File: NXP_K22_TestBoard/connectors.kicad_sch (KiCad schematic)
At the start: 22 parts, among them J301 Barrel_Jack, J302 Conn_ARM_JTAG_SWD_10, J303 PortA, J304 PortB, J305 PortC, J306 PortD, J307 Analog, J308 OLED, J309 UART, J310 Power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

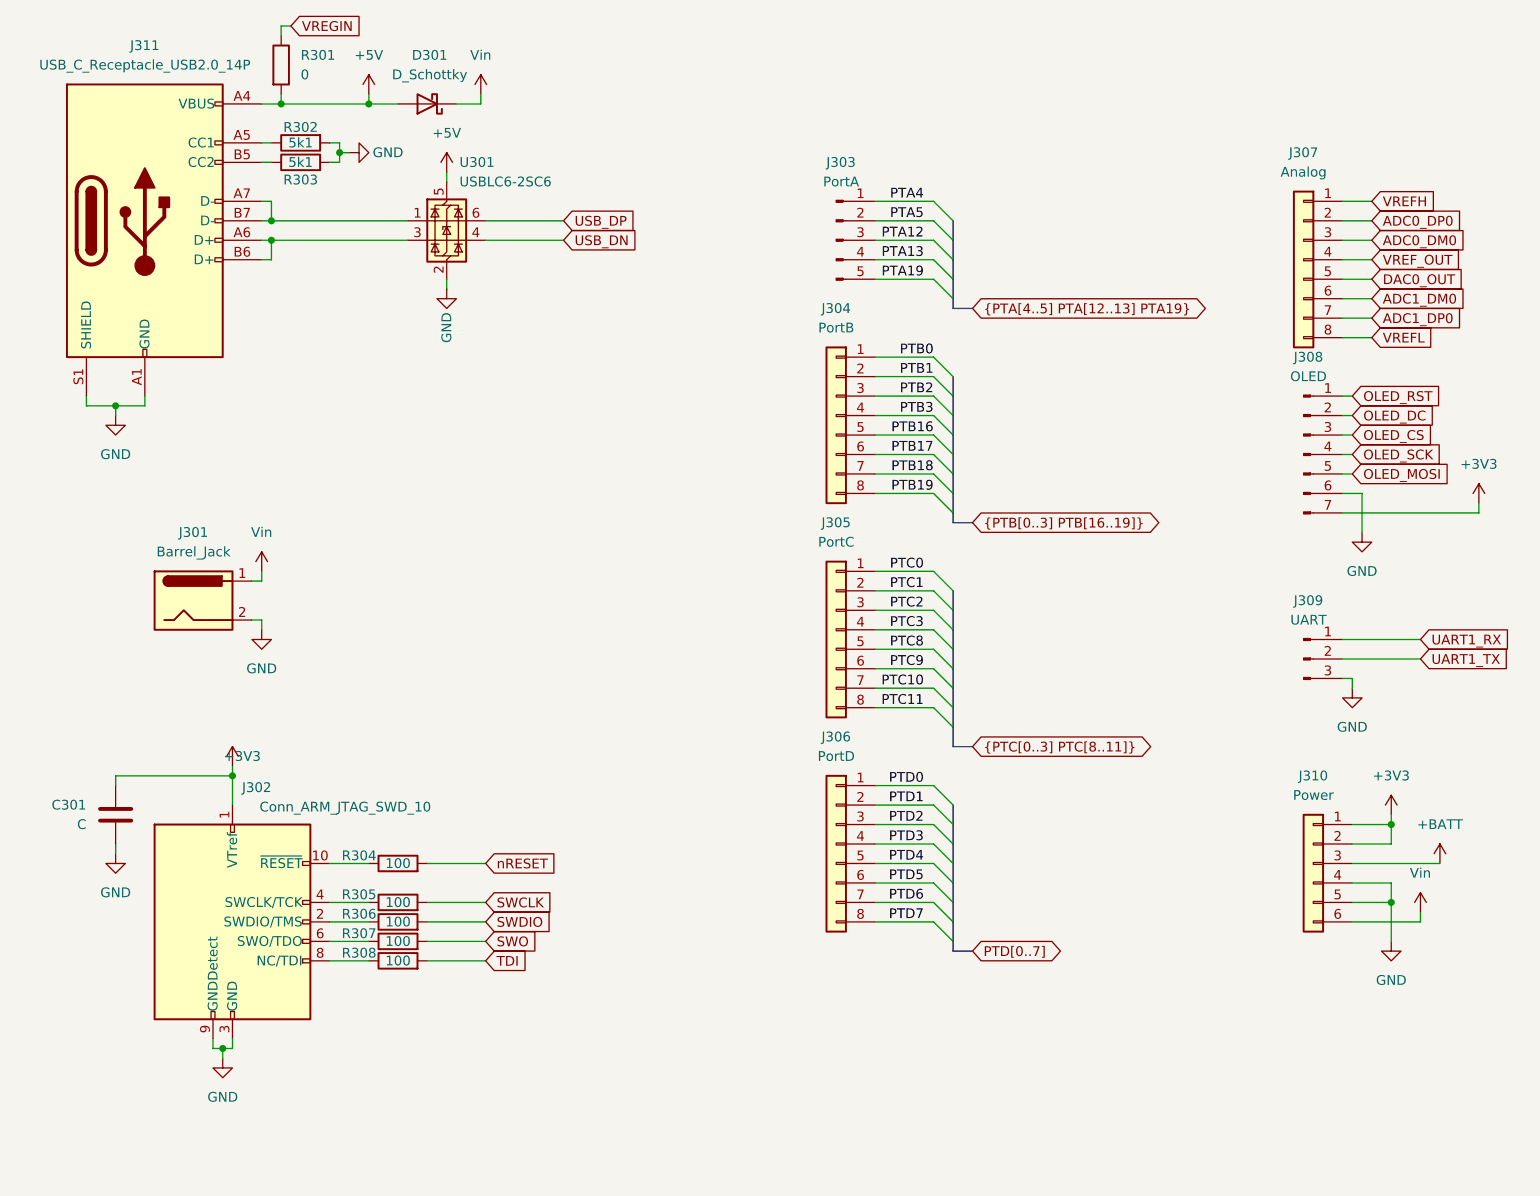
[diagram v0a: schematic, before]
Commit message: Finished board layout
Design rules not checked yet
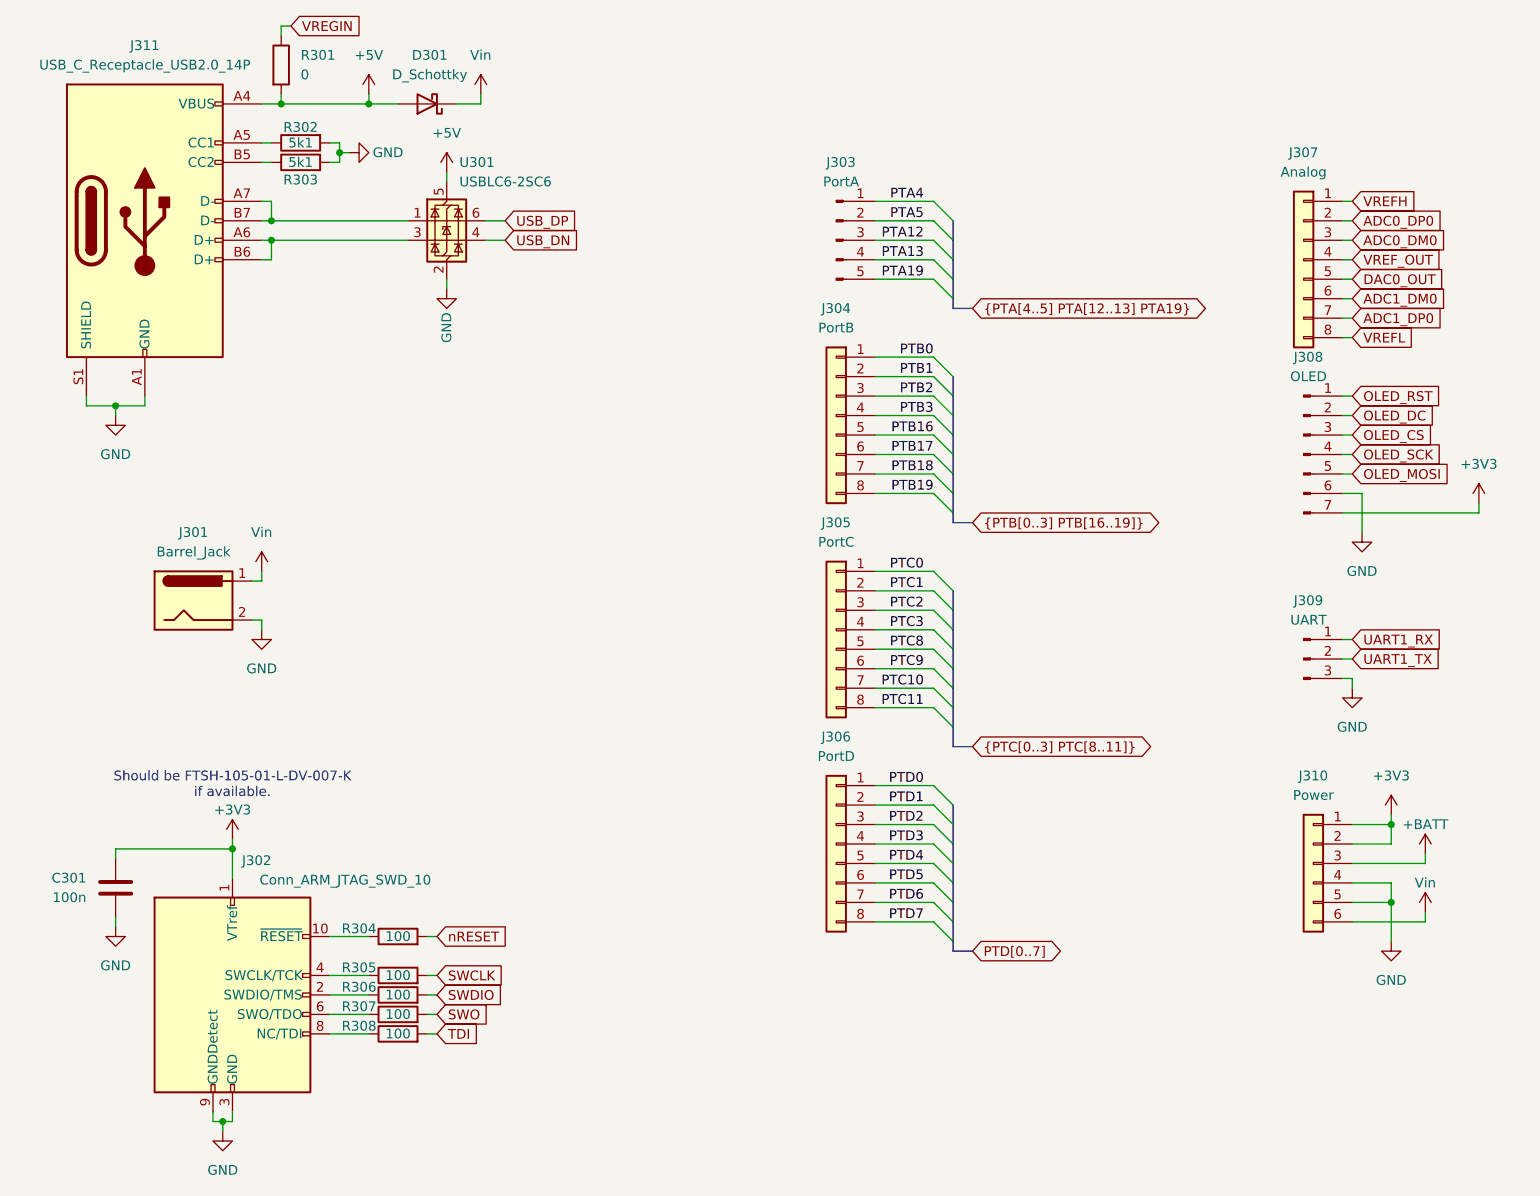
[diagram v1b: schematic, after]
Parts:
- C301: value C -> 100n; MPN (none) -> Generic C/100nF/X7R/16V/0603
- D301: LCSC Part # (none) -> C520634; MPN (none) -> Generic Schottky/10Vr/2A/SOD323-2
- J301: LCSC Part # (none) -> C319133; MPN (none) -> DC-005-5A-2.5-SMT
- J302: Alt LCSC Part # (none) -> C5296739; LCSC Part # (none) -> C5250218; MPN (none) -> FTSH-105-01-F-DV-K-P-TR
- J311: LCSC Part # (none) -> C165948; MPN (none) -> TYPE-C-31-M-12
- R301: MPN (none) -> Generic R/0R/0603
- R302, R303: MPN (none) -> Generic R/5k1/0603
- R304, R305, R306, R307, R308: MPN (none) -> Generic R/100R/0603
- U301: LCSC Part # (none) -> C2827654; MPN (none) -> USBLC6-2SC6
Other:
- note added: "Should be FTSH-105-01-L-DV-007-K if available."
- moved on the sheet: C301, J302, R304, R305, R306, R307, R308
